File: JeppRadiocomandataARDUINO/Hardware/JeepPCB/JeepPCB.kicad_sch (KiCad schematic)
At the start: 17 parts, among them J1 Radio, U1 ATmega328P-A

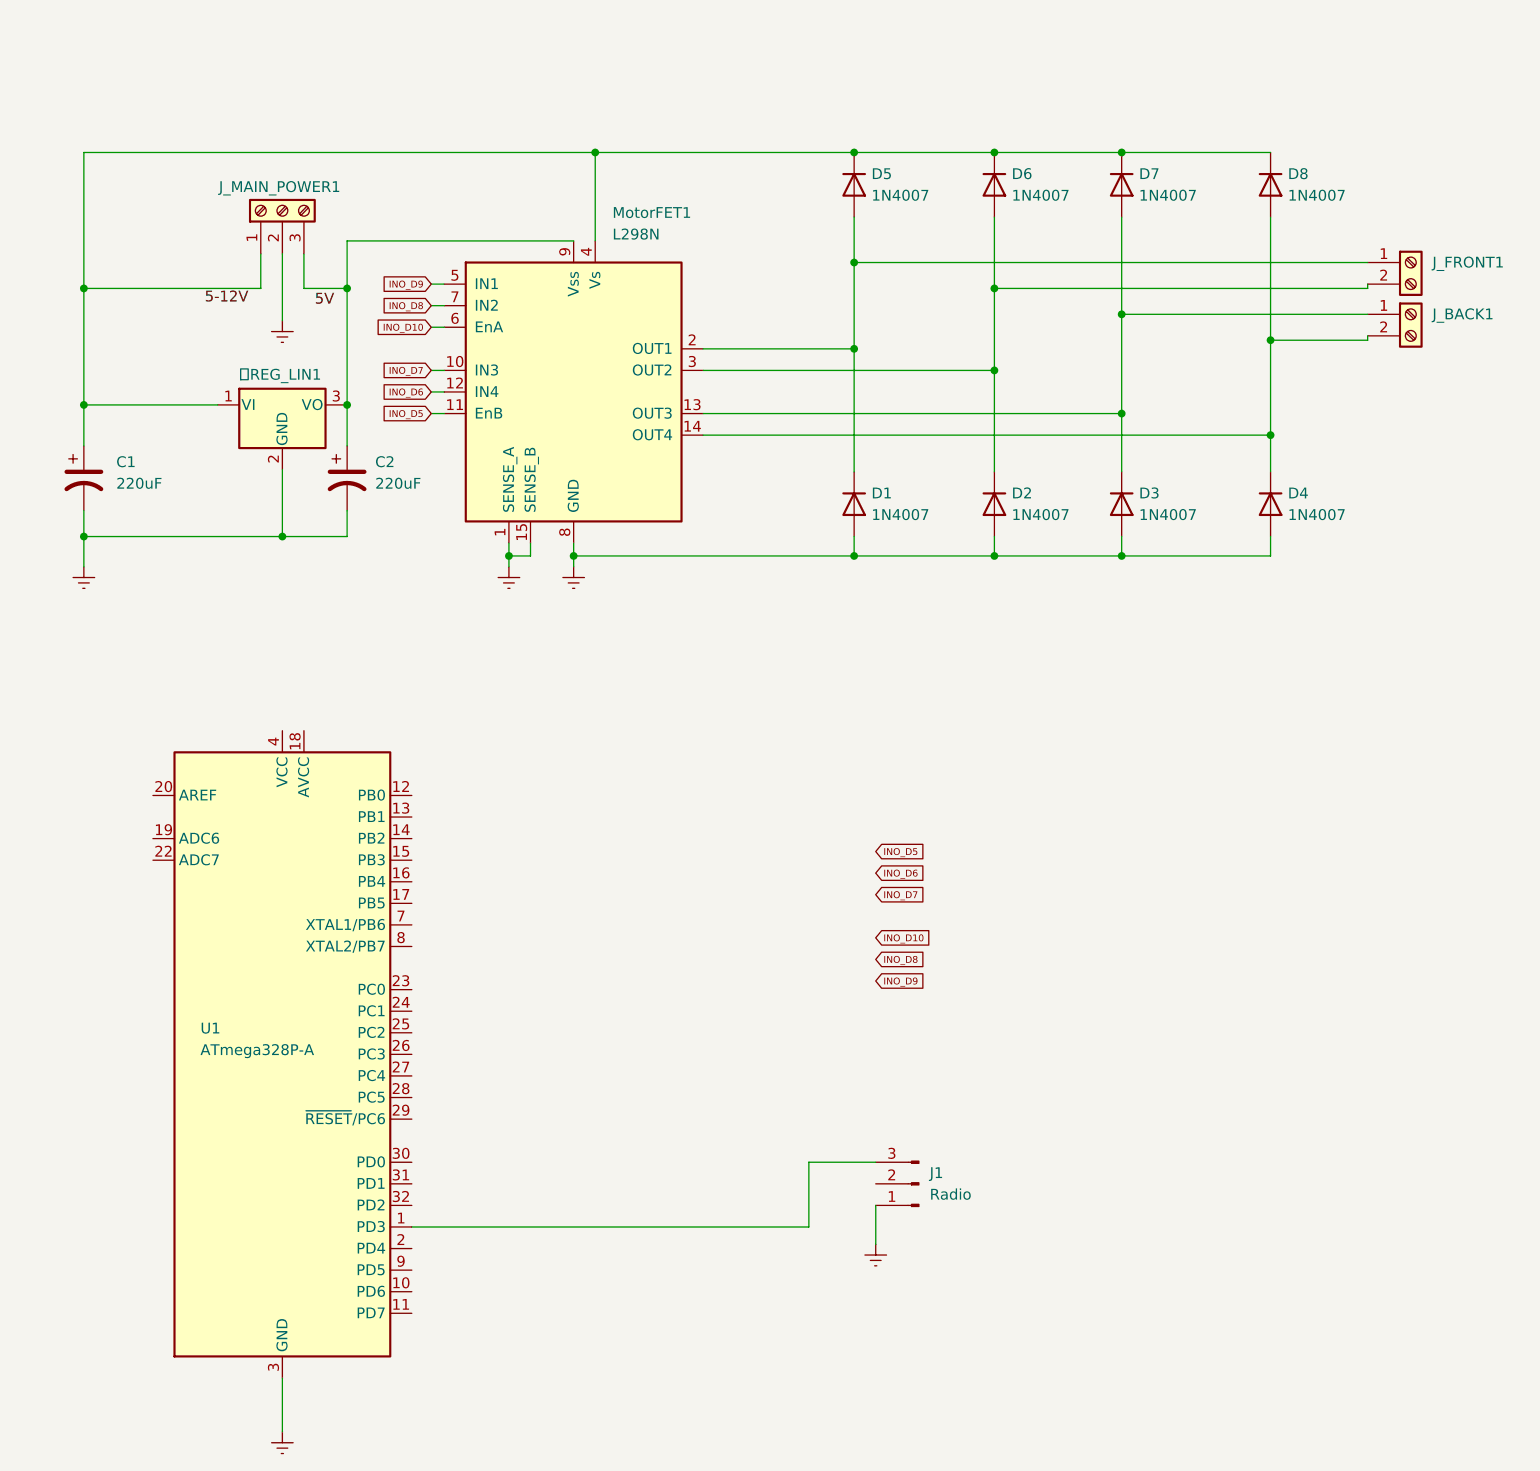
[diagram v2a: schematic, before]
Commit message: Aggiornamento PCB Jeep
Aggiunta delle connessioni necessarie per il processore
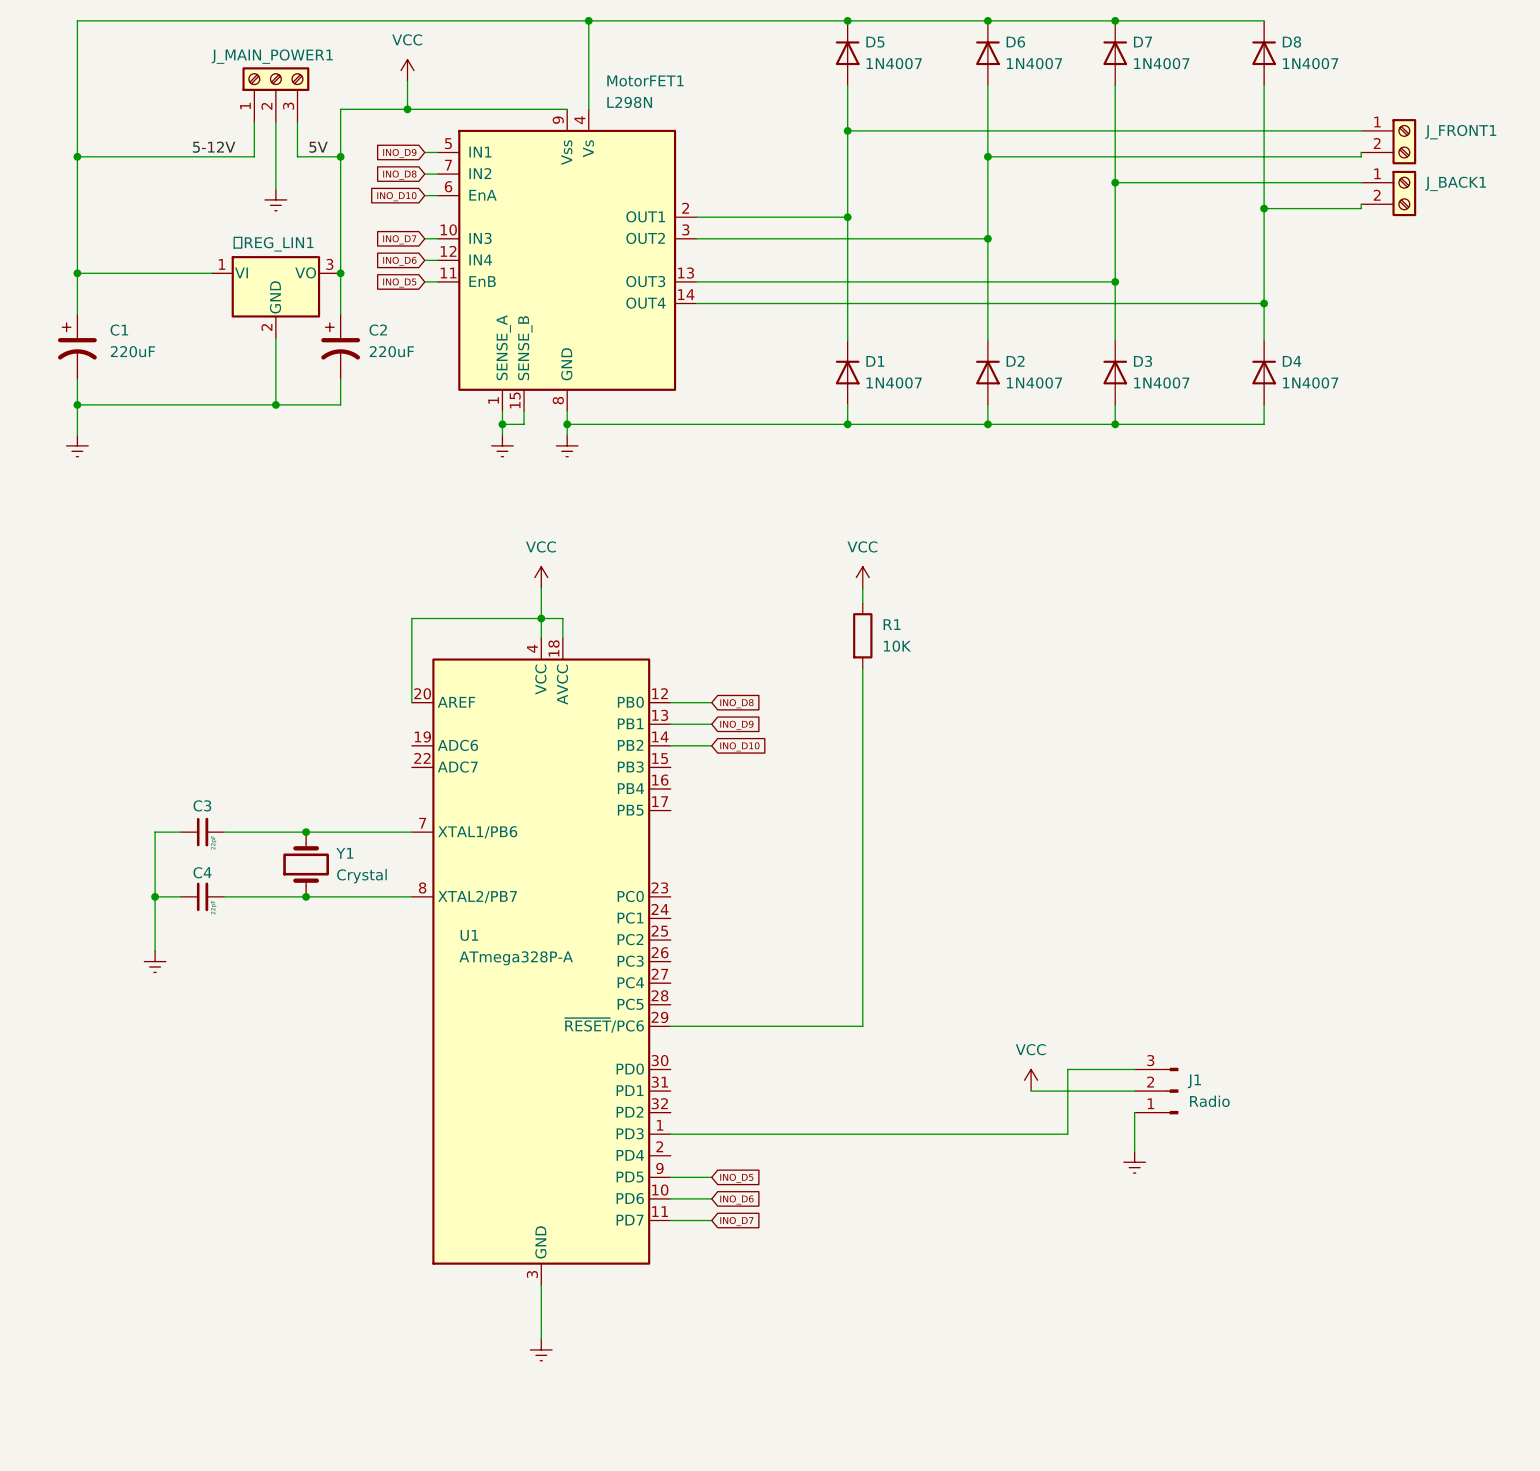
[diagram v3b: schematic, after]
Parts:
- added C3, C4: 22pF, Capacitor_Tantalum_SMD:CP_EIA-1608-10_AVX-L_Pad1.25x1.05mm_HandSolder, symbol Device:C_Small
- added R1: 10K, Resistor_SMD:R_2816_7142Metric_Pad3.20x4.45mm_HandSolder, symbol Device:R
- added Y1: Crystal, Crystal:Crystal_SMD_0603-2Pin_6.0x3.5mm, symbol Device:Crystal
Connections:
- net 5-12V: now also REG_LIN1.1 (VI), C1.1, D5.1 (K), D6.1 (K), D7.1 (K), D8.1 (K), J_MAIN_POWER1.1 (Pin_1), MotorFET1.4 (Vs)
- net Earth: now also C3.1, C4.1
- net INO_D10: now also U1.14 (PB2)
- net INO_D5: now also U1.9 (PD5)
- net INO_D6: now also U1.10 (PD6)
- net INO_D7: now also U1.11 (PD7)
- net INO_D8: now also U1.12 (PB0)
- net INO_D9: now also U1.13 (PB1)
- net VCC: now reaches REG_LIN1.3 (VO), C2.1, J_MAIN_POWER1.3 (Pin_3), MotorFET1.9 (Vss)
- net VCC: now also J1.2 (Pin_2), U1.18 (AVCC), U1.20 (AREF), U1.4 (VCC), U1.6 (VCC), R1.1
- net at U1.29 (~{RESET}/PC6): now also R1.2
- net at U1.7 (XTAL1/PB6): now also C3.2, Y1.2
- net at U1.8 (XTAL2/PB7): now also C4.2, Y1.1
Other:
- moved on the sheet: REG_LIN1, C1, C2, D1, D2, D3, D4, D5, D6, D7, D8, J1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

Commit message: Aggiornamento della resistenza da 10K e posizionamento dei componenti
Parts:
- R1: footprint Resistor_SMD:R_2816_7142Metric_Pad3.20x4.45mm_HandSolder -> Resistor_SMD:R_0402_1005Metric
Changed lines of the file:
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@@
       (effects (font (size 1.27 1.27)) (justify left))
     )
-    (property "Footprint" "Resistor_SMD:R_2816_7142Metric_Pad3.20x4.45mm_HandSolder" (id 2) (at 115.316 91.694 90)
+    (property "Footprint" "Resistor_SMD:R_0402_1005Metric" (id 2) (at 115.316 91.694 90)
       (effects (font (size 1.27 1.27)) hide)
     )
@@
     )
     (path "/f34be8ea-310f-4294-8838-87279f7f3ffa"
-      (reference "R1") (unit 1) (value "10K") (footprint "Resistor_SMD:R_2816_7142Metric_Pad3.20x4.45mm_HandSolder")
+      (reference "R1") (unit 1) (value "10K") (footprint "Resistor_SMD:R_0402_1005Metric")
     )
     (path "/c751029c-0ca6-4cd0-8725-946b9af36995"

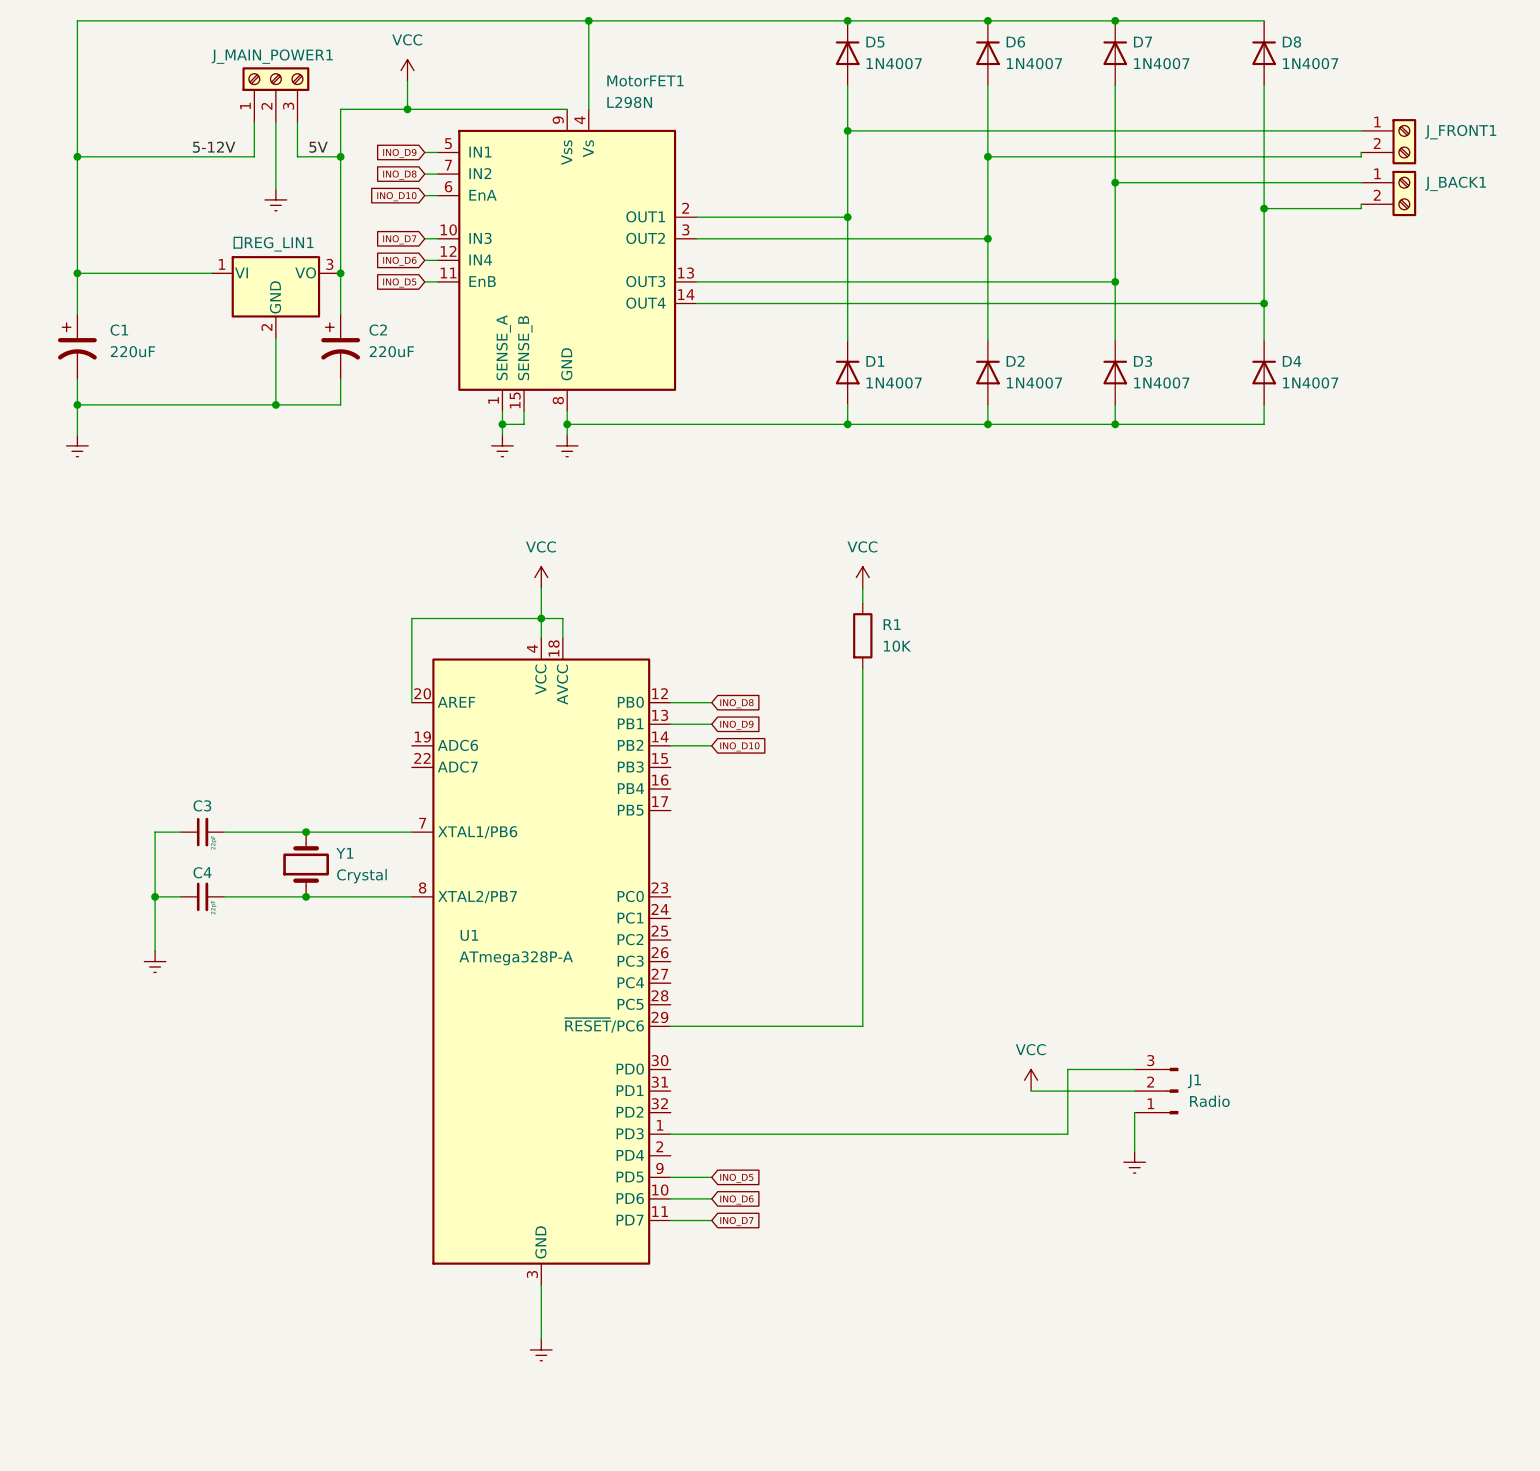
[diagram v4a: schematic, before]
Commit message: Collegamento delle tracce
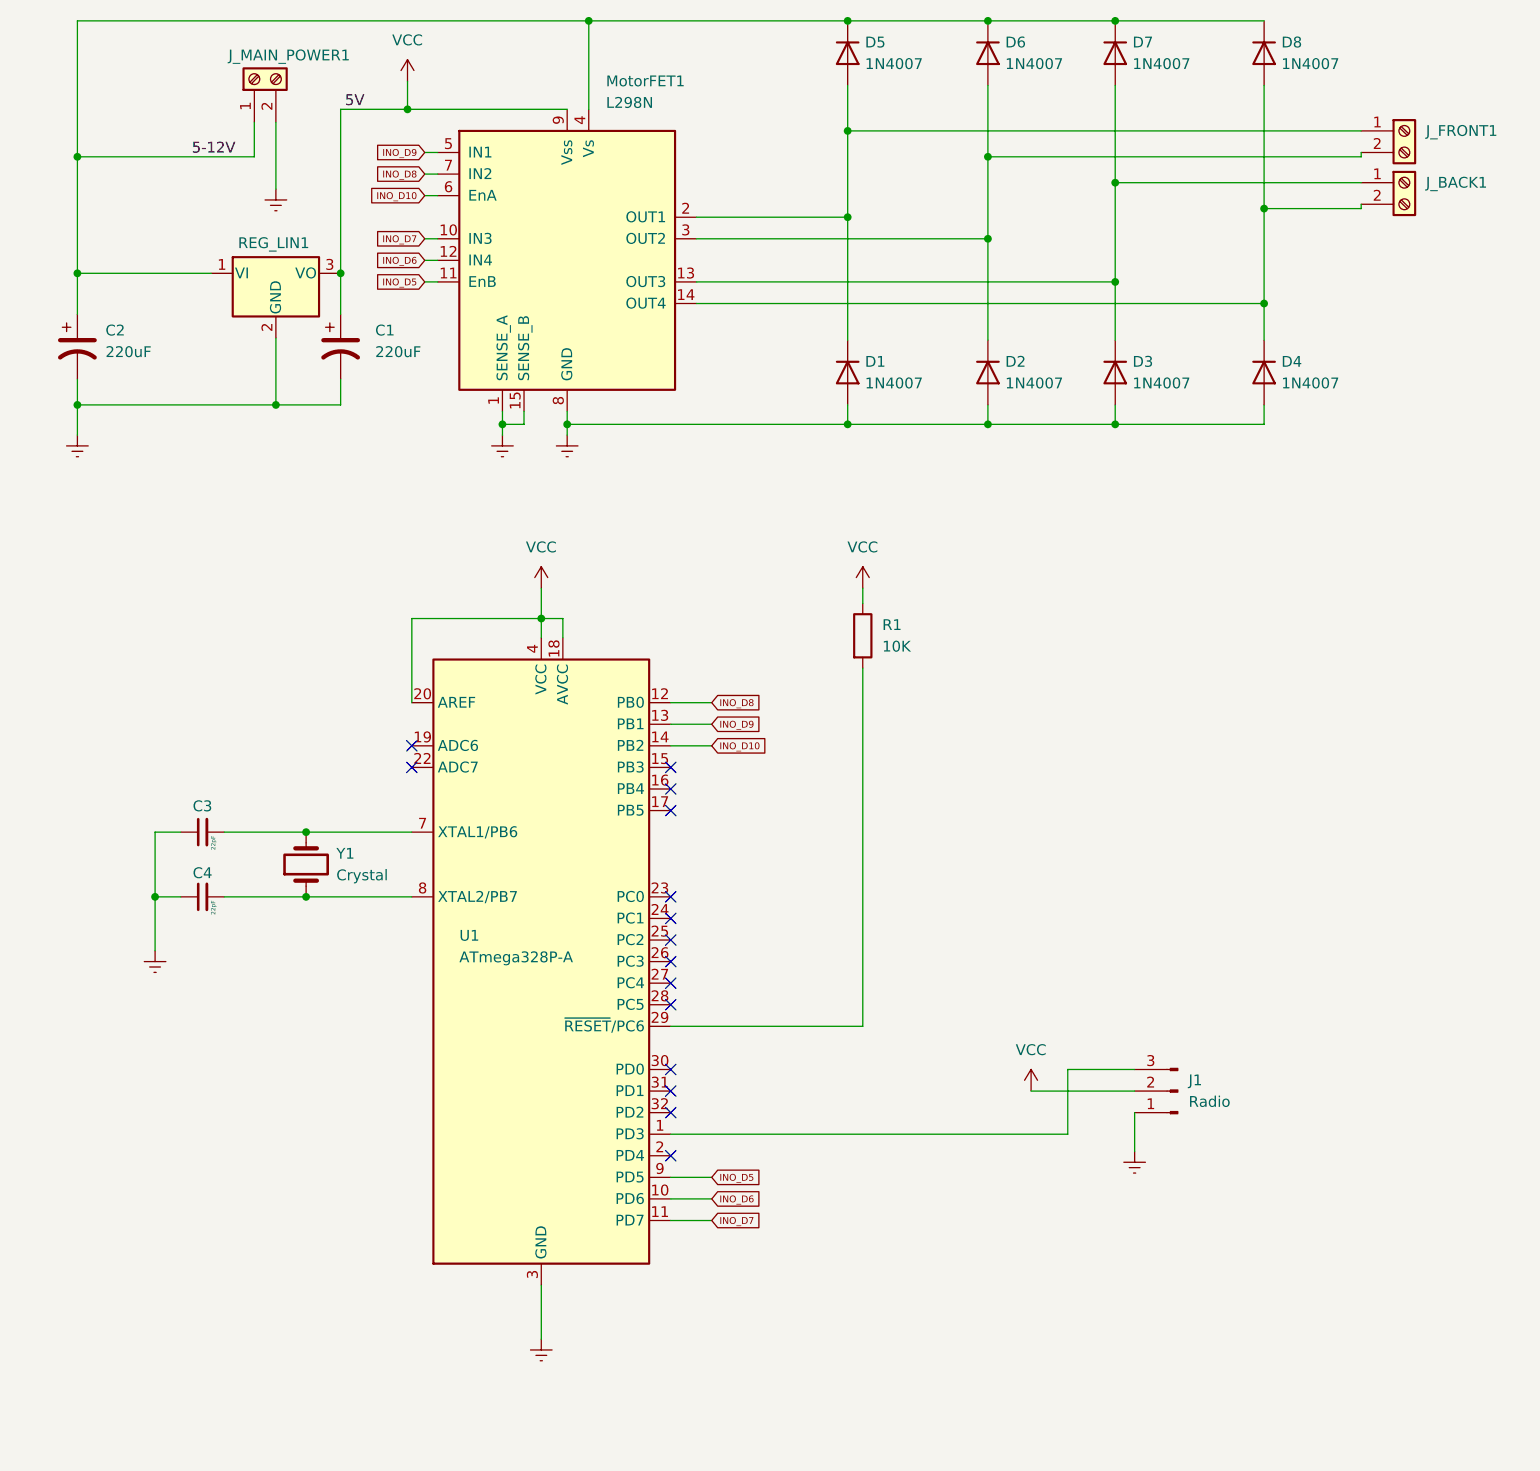
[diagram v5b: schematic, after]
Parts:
- removed J_MAIN_POWER1: Screw_Terminal_01x03, TerminalBlock_Phoenix:TerminalBlock_Phoenix_MKDS-1,5-3_1x03_P5.00mm_Horizontal, symbol Connector:Screw_Terminal_01x03
- added J_MAIN_POWER1: Screw_Terminal_01x02, TerminalBlock_Phoenix:TerminalBlock_Phoenix_MKDS-1,5-2-5.08_1x02_P5.08mm_Horizontal, symbol Connector:Screw_Terminal_01x02
- D1, D2, D3, D4, D5, D6, D7, D8: footprint Diode_SMD:D_0402_1005Metric_Pad0.77x0.64mm_HandSolder -> Diode_SMD:D_MicroMELF_Handsoldering
- renumbered C2 to C1, C1 to C2, REG_LIN1 to REG_LIN1
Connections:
- net 5-12V: now also J_MAIN_POWER1.1 (Pin_1)
- net Earth: now also J_MAIN_POWER1.2 (Pin_2)
- no-connect marks 0 -> 15
